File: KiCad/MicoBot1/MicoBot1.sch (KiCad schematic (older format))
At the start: 21 parts, among them J1 Conn_01x04_Male, J2 Bat, J3 Motor2, J4 Motor1, J5 Conn_01x04_Male, J6 Conn_01x06_Male, J7 Conn_01x03_Male, J8 Conn_01x06_Male, SW1 Rst, SW2 On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

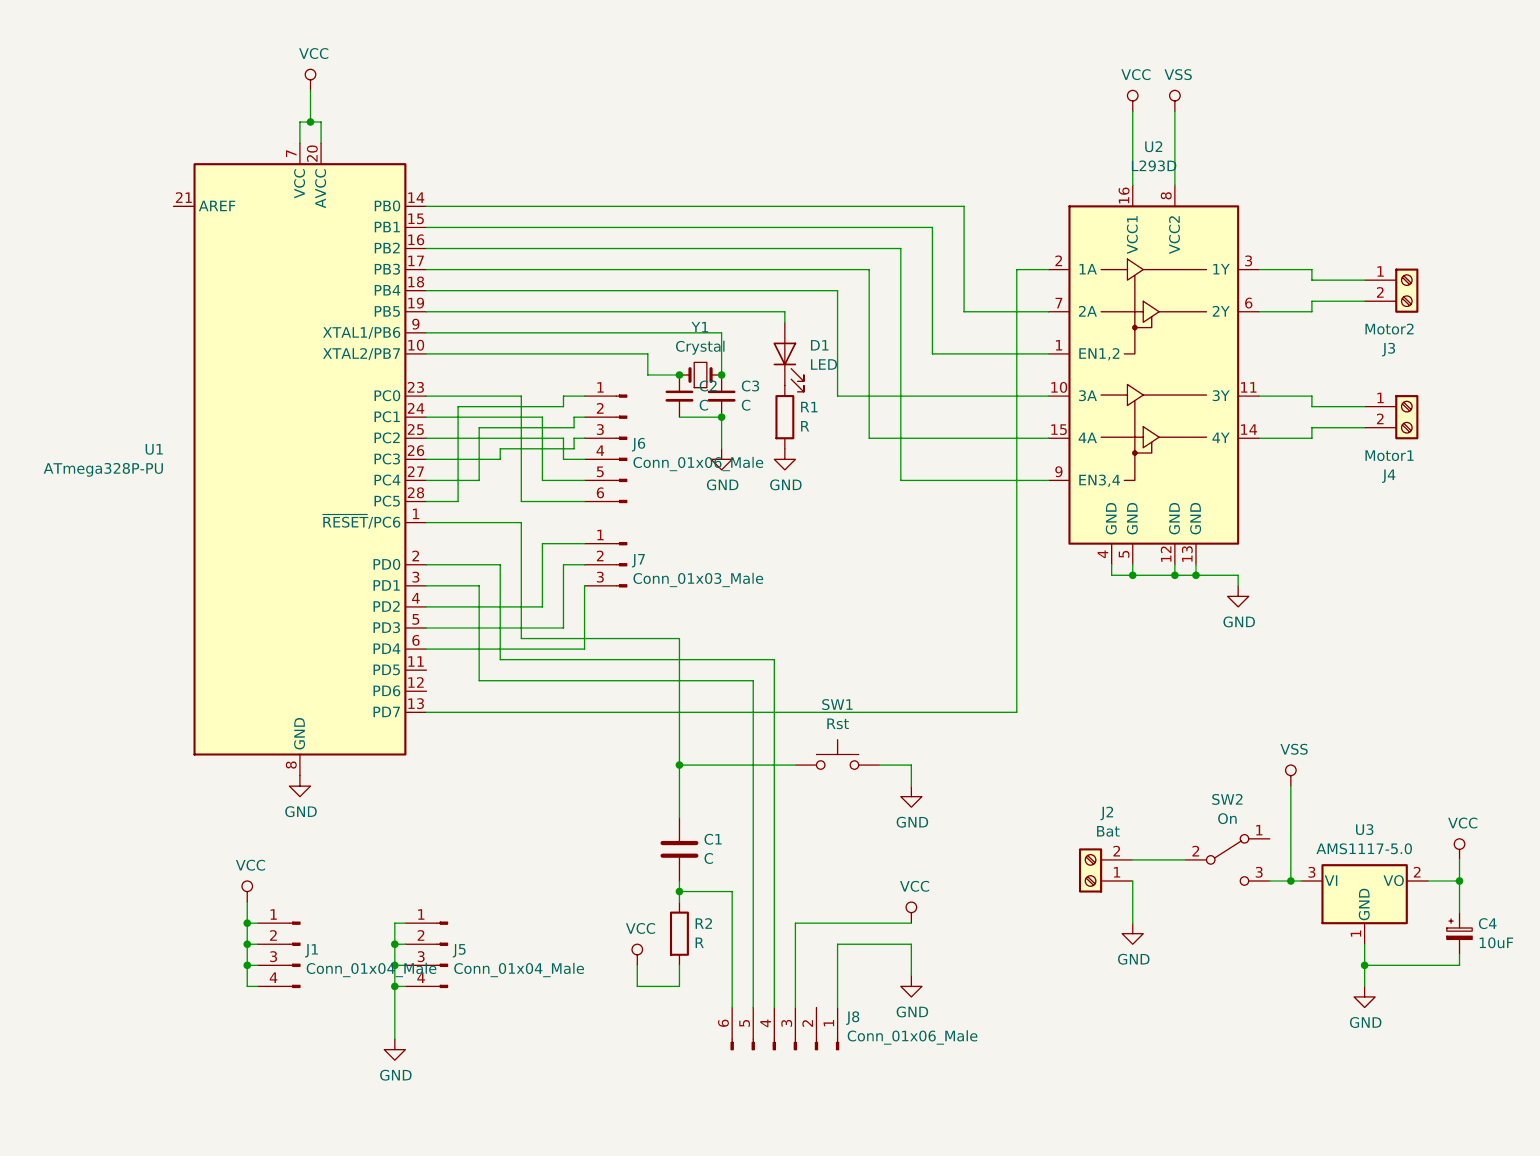
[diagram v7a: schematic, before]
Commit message: 
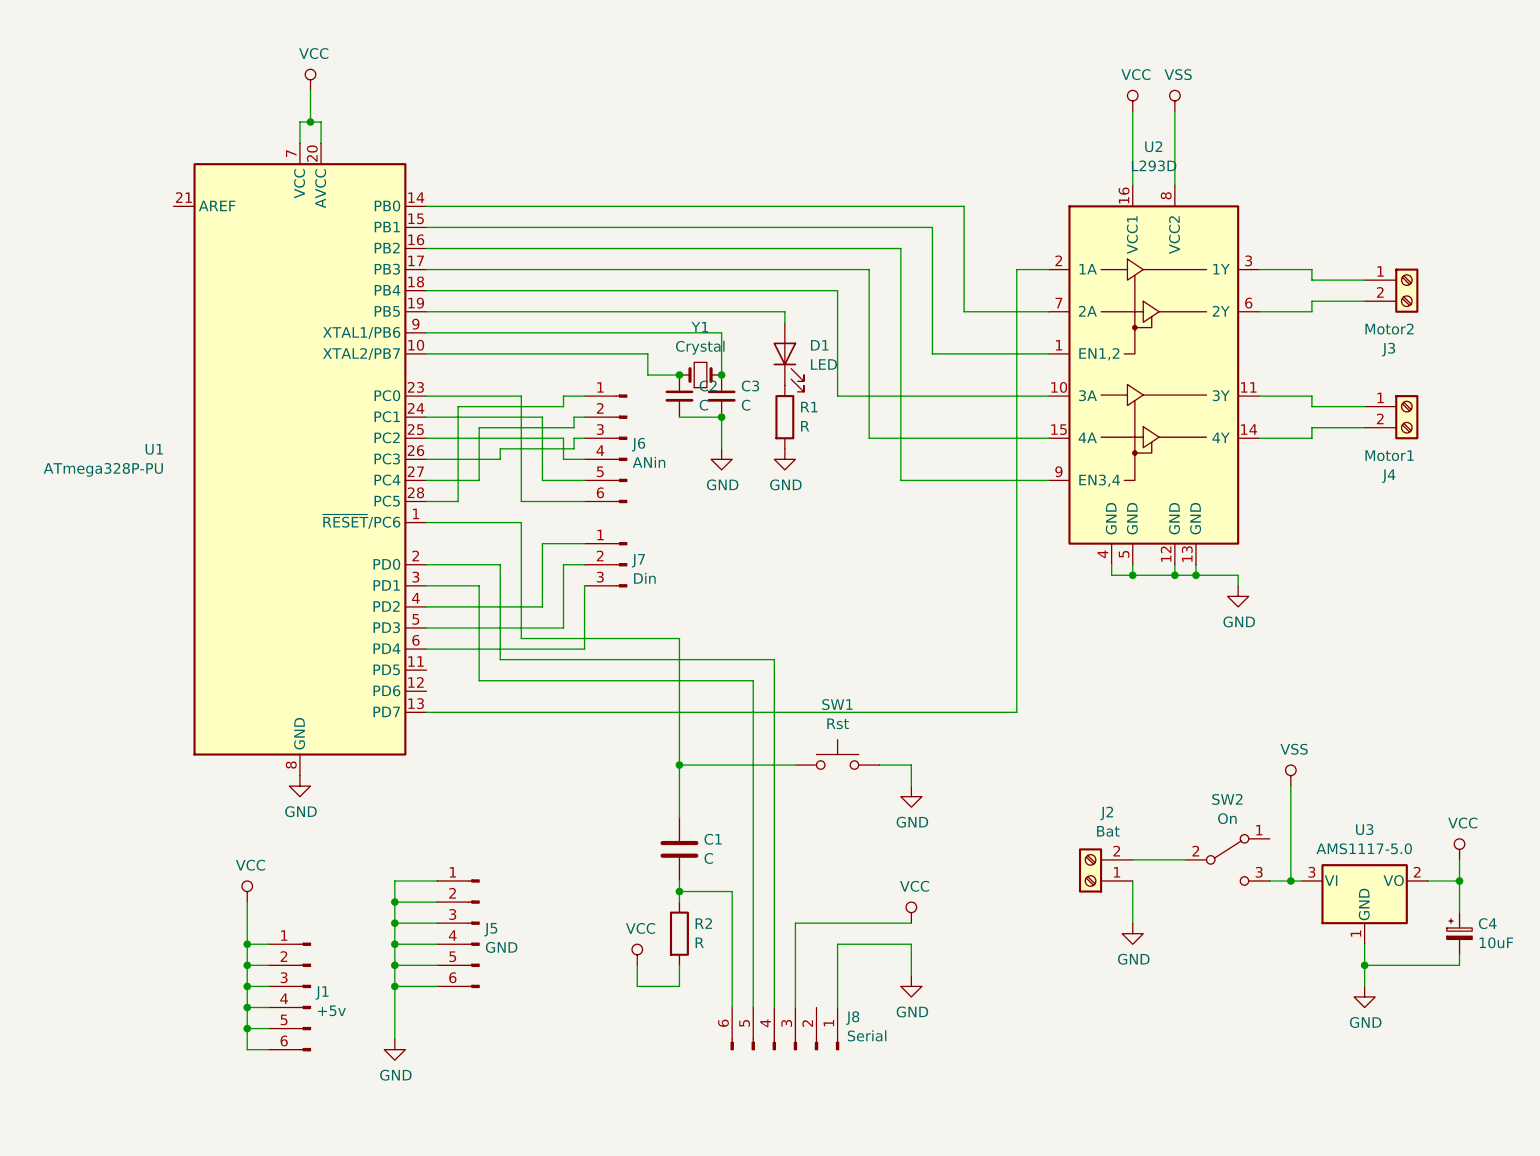
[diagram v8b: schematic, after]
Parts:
- removed J1, J5: Conn_01x04_Male, Connector_PinHeader_2.54mm:PinHeader_1x04_P2.54mm_Vertical, symbol Connector:Conn_01x04_Male
- added J1: +5v, Connector_PinHeader_2.54mm:PinHeader_1x06_P2.54mm_Vertical, symbol Connector:Conn_01x06_Male
- added J5: GND, Connector_PinHeader_2.54mm:PinHeader_1x06_P2.54mm_Vertical, symbol Connector:Conn_01x06_Male
- J6: value Conn_01x06_Male -> ANin
- J7: value Conn_01x03_Male -> Din
- J8: value Conn_01x06_Male -> Serial
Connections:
- net GND: now also J5.1 (Pin_1), J5.2 (Pin_2), J5.3 (Pin_3), J5.4 (Pin_4), J5.5 (Pin_5), J5.6 (Pin_6)
- net VCC: now also J1.1 (Pin_1), J1.2 (Pin_2), J1.3 (Pin_3), J1.4 (Pin_4), J1.5 (Pin_5), J1.6 (Pin_6)
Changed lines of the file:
@@
 	1    0    0    -1
 $EndComp
-Wire Wire Line
-	4050 5450 4000 5450
-Wire Wire Line
-	4050 5350 4000 5350
-Wire Wire Line
-	4000 5350 4000 5450
-Wire Wire Line
-	4050 5250 4000 5250
-Wire Wire Line
-	4000 5250 4000 5350
-Connection ~ 4000 5350
-Wire Wire Line
-	4050 5150 4000 5150
-Wire Wire Line
-	4000 5150 4000 5250
-Connection ~ 4000 5250
 $Comp
 L Device:R R2
@@
 Wire Wire Line
 	4700 3350 4900 3350
-Wire Wire Line
-	3300 5050 3300 5150
-Wire Wire Line
-	3300 5450 3350 5450
-Wire Wire Line
-	3300 5350 3350 5350
-Connection ~ 3300 5350
-Wire Wire Line
-	3300 5350 3300 5450
-Wire Wire Line
-	3300 5250 3350 5250
-Connection ~ 3300 5250
-Wire Wire Line
-	3300 5250 3300 5350
-Wire Wire Line
-	3300 5150 3350 5150
-Connection ~ 3300 5150
-Wire Wire Line
-	3300 5150 3300 5250
-Wire Wire Line
-	4000 5450 4000 5700
-Connection ~ 4000 5450
 $Comp
 L Connector:Conn_01x06_Male J8
@@
 P 5900 5750
 F 0 "J8" V 6054 5994 50  0000 L CNN
-F 1 "Conn_01x06_Male" V 5963 5994 50  0000 L CNN
+F 1 "Serial" V 5963 5994 50  0000 L CNN
 F 2 "Connector_PinHeader_2.54mm:PinHeader_1x06_P2.54mm_Vertical" H 5900 5750 50  0001 C CNN
 F 3 "~" H 5900 5750 50  0001 C CNN
@@
 $EndComp
 $Comp
-L Connector:Conn_01x04_Male J5
-U 1 1 5D6D911B
-P 4250 5250
-F 0 "J5" H 4222 5224 50  0000 R CNN
-F 1 "Conn_01x04_Male" H 4222 5133 50  0000 R CNN
-F 2 "Connector_PinHeader_2.54mm:PinHeader_1x04_P2.54mm_Vertical" H 4250 5250 50  0001 C CNN
-F 3 "~" H 4250 5250 50  0001 C CNN
-	1    4250 5250
-	-1   0    0    -1
-$EndComp
-$Comp
-L Connector:Conn_01x04_Male J1
-U 1 1 5D6D9FD3
-P 3550 5250
-F 0 "J1" H 3522 5224 50  0000 R CNN
-F 1 "Conn_01x04_Male" H 3522 5133 50  0000 R CNN
-F 2 "Connector_PinHeader_2.54mm:PinHeader_1x04_P2.54mm_Vertical" H 3550 5250 50  0001 C CNN
-F 3 "~" H 3550 5250 50  0001 C CNN
-	1    3550 5250
-	-1   0    0    -1
-$EndComp
-$Comp
 L Connector:Conn_01x03_Male J7
 U 1 1 5D6E1400
 P 5100 3450
 F 0 "J7" H 5072 3474 50  0000 R CNN
-F 1 "Conn_01x03_Male" H 5072 3383 50  0000 R CNN
+F 1 "Din" H 5072 3383 50  0000 R CNN
 F 2 "Connector_PinHeader_2.54mm:PinHeader_1x03_P2.54mm_Vertical" H 5100 3450 50  0001 C CNN
 F 3 "~" H 5100 3450 50  0001 C CNN
@@
 P 5100 2850
 F 0 "J6" H 5072 2824 50  0000 R CNN
-F 1 "Conn_01x06_Male" H 5072 2733 50  0000 R CNN
+F 1 "ANin" H 5072 2733 50  0000 R CNN
 F 2 "Connector_PinHeader_2.54mm:PinHeader_1x06_P2.54mm_Vertical" H 5100 2850 50  0001 C CNN
 F 3 "~" H 5100 2850 50  0001 C CNN
@@
 	-1   0    0    -1
 $EndComp
+Wire Wire Line
+	3300 5050 3300 5250
+Wire Wire Line
+	4000 5150 4000 5250
+$Comp
+L Connector:Conn_01x06_Male J1
+U 1 1 5D566BB2
+P 3600 5450
+F 0 "J1" H 3572 5424 50  0000 R CNN
+F 1 "+5v" H 3572 5333 50  0000 R CNN
+F 2 "Connector_PinHeader_2.54mm:PinHeader_1x06_P2.54mm_Vertical" H 3600 5450 50  0001 C CNN
+F 3 "~" H 3600 5450 50  0001 C CNN
+	1    3600 5450
+	-1   0    0    -1
+$EndComp
+$Comp
+L Connector:Conn_01x06_Male J5
+U 1 1 5D5683CC
+P 4400 5150
+F 0 "J5" H 4372 5124 50  0000 R CNN
+F 1 "GND" H 4372 5033 50  0000 R CNN
+F 2 "Connector_PinHeader_2.54mm:PinHeader_1x06_P2.54mm_Vertical" H 4400 5150 50  0001 C CNN
+F 3 "~" H 4400 5150 50  0001 C CNN
+	1    4400 5150
+	-1   0    0    -1
+$EndComp
+Wire Wire Line
+	3400 5250 3300 5250
+Connection ~ 3300 5250
+Wire Wire Line
+	3300 5250 3300 5350
+Wire Wire Line
+	3400 5350 3300 5350
+Connection ~ 3300 5350
+Wire Wire Line
+	3300 5350 3300 5450
+Wire Wire Line
+	3300 5450 3400 5450
+Wire Wire Line
+	3400 5550 3300 5550
+Wire Wire Line
+	3300 5550 3300 5450
+Connection ~ 3300 5450
+Wire Wire Line
+	3400 5650 3300 5650
+Wire Wire Line
+	3300 5650 3300 5550
+Connection ~ 3300 5550
+Wire Wire Line
+	3400 5750 3300 5750
+Wire Wire Line
+	3300 5750 3300 5650
+Connection ~ 3300 5650
+Wire Wire Line
+	4000 5150 4200 5150
+Wire Wire Line
+	4000 5150 4000 5050
+Wire Wire Line
+	4000 5050 4200 5050
+Connection ~ 4000 5150
+Wire Wire Line
+	4000 5050 4000 4950
+Wire Wire Line
+	4000 4950 4200 4950
+Connection ~ 4000 5050
+Wire Wire Line
+	4000 5250 4200 5250
+Connection ~ 4000 5250
+Wire Wire Line
+	4000 5250 4000 5350
+Wire Wire Line
+	4000 5350 4200 5350
+Connection ~ 4000 5350
+Wire Wire Line
+	4000 5350 4000 5450
+Wire Wire Line
+	4000 5450 4200 5450
+Connection ~ 4000 5450
+Wire Wire Line
+	4000 5450 4000 5700
 $EndSCHEMATC
